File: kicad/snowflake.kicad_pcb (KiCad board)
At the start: 2 copper layers, 123.3 x 86 mm, 62 parts

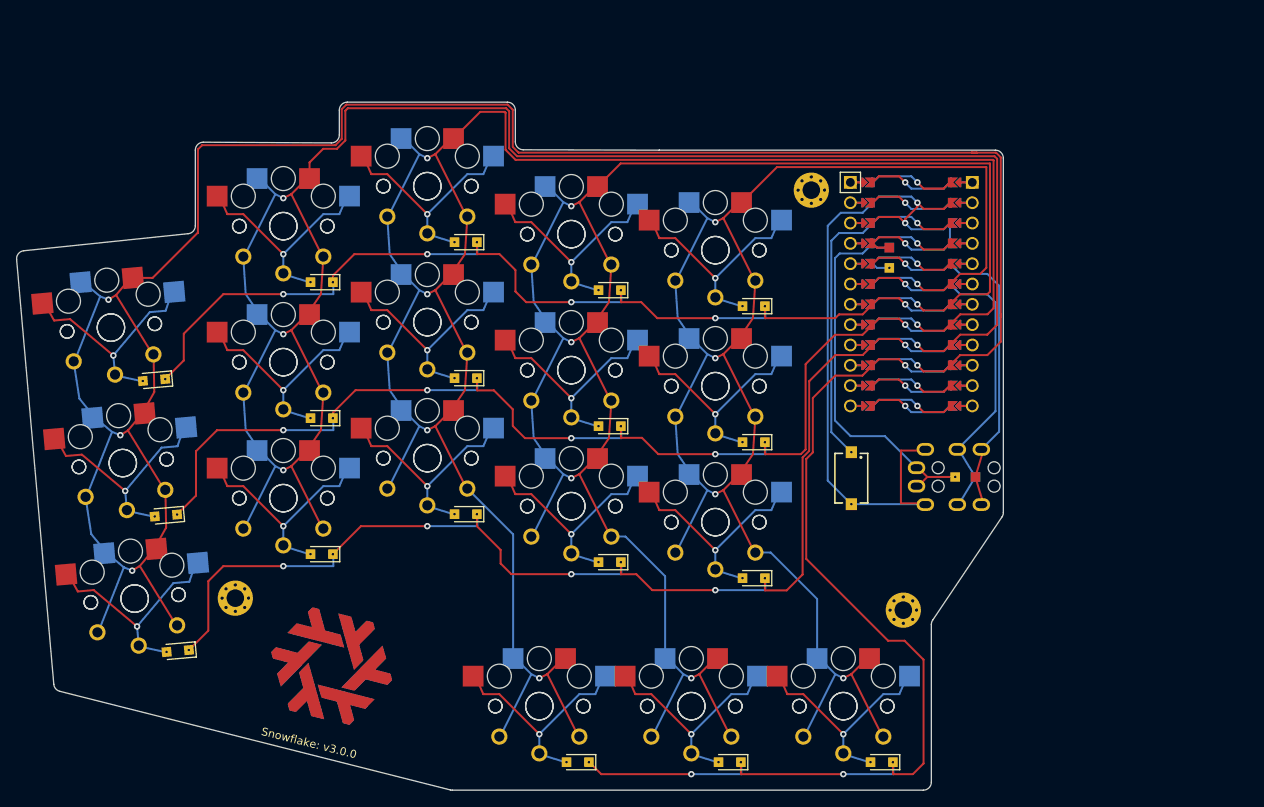
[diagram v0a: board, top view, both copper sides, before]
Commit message: chore: backup
I am not done with these changes but am about to wipe my computer.
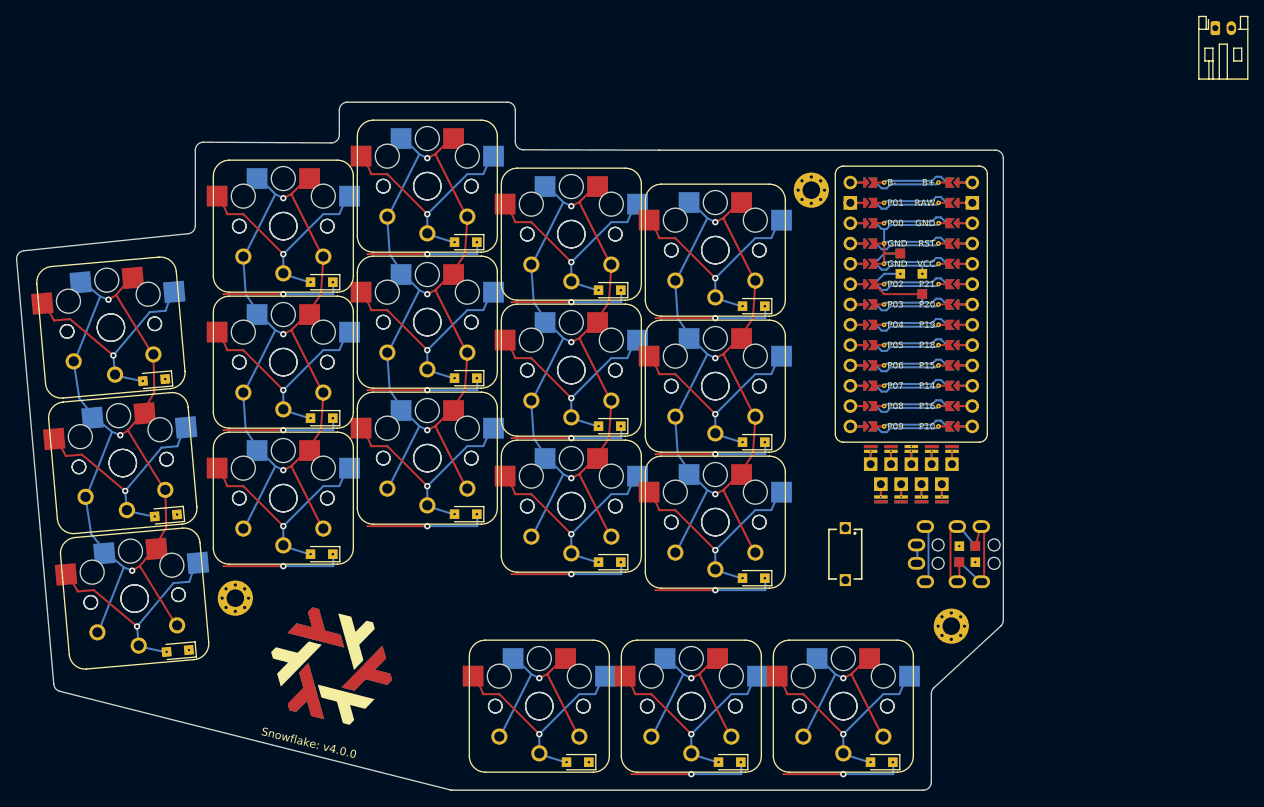
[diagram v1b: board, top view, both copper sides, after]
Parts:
- removed MCU1: , ProMicro
- removed S37: , PG1350
- removed _2, _3: , MountingHole_2.2mm_M2_Pad_Via
- added ?: , 434121025816,  at (188.8, 94.5)
- added ?: , nice!view,  at (197.1, 83.2)
- added ?: , ssd1306,  at (197.1, 85.7)
- added _10: , MountingHole_2.2mm_M2_Pad_Via,  at (202.1, 103.5)
- added _11: , MountingHole_2.2mm_M2_Pad_Via,  at (112.6, 100.0)
- added _9: , MountingHole_2.2mm_M2_Pad_Via,  at (184.6, 49.0)
- added nice!nano1: , nice!nano,  at (197.1, 60.7)
- added threeWayJumper3: Jumper, Jumper_1TH_2SMD, F.Cu at (204.1, 93.5)
- added threeWayJumper4: Jumper, Jumper_1TH_2SMD, F.Cu at (204.1, 95.5)
- D1, D10, D11, D12, D13, D14, D15, D16, D17, D18, D2, D3, D4, D5, D6, D7, D8, D9: moved to 
- S1: footprint 434121025816 -> PG1350
- _1: footprint MountingHole_2.2mm_M2_Pad_Via -> Connector_JST:JST_PH_S2B-PH-K_1x02_P2.00mm_Horizontal; moved to 
- moved S1 90.8 mm to (100.0, 100.0), turned to 5 degrees
- moved S19 89.6 mm to (100.0, 100.0), turned to 185 degrees
- moved S16 61.1 mm to (150.6, 113.5)
- moved S34 61.1 mm to (150.6, 113.5)
- moved _1 54.4 mm to (235.1, 28.7)
- moved S10 43.9 mm to (154.6, 88.5)
- moved S28 43.9 mm to (154.6, 88.5)
- moved S13 40.2 mm to (172.6, 90.5)
- moved S31 40.2 mm to (172.6, 90.5)
- moved S25 34.1 mm to (136.6, 82.5)
- moved S7 34.1 mm to (136.6, 82.5)
- moved S22 30.3 mm to (118.6, 87.5), turned to 180 degrees
- moved S4 30.3 mm to (118.6, 87.5), turned to 0 degrees
- moved threeWayJumper2 24.7 mm to (198.5, 60.7), turned to 270 degrees
- moved S17 19.0 mm to (169.6, 113.5)
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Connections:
- net P4 renamed P08
- net P5 renamed P09
- D1 pad 1: P6 -> P10
- D10 pad 1: P6 -> P10
- D13 pad 1: P6 -> P10
- D16 pad 1: P7 -> P16
- D17 pad 1: P7 -> P16
- D18 pad 1: P7 -> P16
- D4 pad 1: P6 -> P10
- D7 pad 1: P6 -> P10
- S1 pad 1: RST -> P14
- S1 pad 2: GND -> matrix_pinky_bottom
- S10 pad 1: P18 -> P19
- S10 pad 2: matrix_middle_top -> matrix_index_bottom
- S11 pad 2: matrix_index_bottom -> matrix_index_home
- S12 pad 2: matrix_index_home -> matrix_index_top
- S13 pad 1: P19 -> P20
- S13 pad 2: matrix_index_top -> matrix_inner_bottom
- S14 pad 2: matrix_inner_bottom -> matrix_inner_home
- S15 pad 2: matrix_inner_home -> matrix_inner_top
- S16 pad 1: P20 -> P18
- S16 pad 2: matrix_inner_top -> thumbfan_near_thumb
- S17 pad 1: P18 -> P19
- S17 pad 2: thumbfan_near_thumb -> thumbfan_home_thumb
- S18 pad 1: P19 -> P20
- S18 pad 2: thumbfan_home_thumb -> thumbfan_far_thumb
- S19 pad 1: P20 -> P14
- S19 pad 2: thumbfan_far_thumb -> matrix_pinky_bottom
- S2 pad 2: matrix_pinky_bottom -> matrix_pinky_home
- S20 pad 2: matrix_pinky_bottom -> matrix_pinky_home
- S21 pad 2: matrix_pinky_home -> matrix_pinky_top
- S22 pad 1: P14 -> P15
- S22 pad 2: matrix_pinky_top -> matrix_ring_bottom
- S23 pad 2: matrix_ring_bottom -> matrix_ring_home
- S24 pad 2: matrix_ring_home -> matrix_ring_top
- S25 pad 1: P15 -> P18
- S25 pad 2: matrix_ring_top -> matrix_middle_bottom
- S26 pad 2: matrix_middle_bottom -> matrix_middle_home
- S27 pad 2: matrix_middle_home -> matrix_middle_top
- S28 pad 1: P18 -> P19
- S28 pad 2: matrix_middle_top -> matrix_index_bottom
- S29 pad 2: matrix_index_bottom -> matrix_index_home
- S3 pad 2: matrix_pinky_home -> matrix_pinky_top
- S30 pad 2: matrix_index_home -> matrix_index_top
- S31 pad 1: P19 -> P20
- S31 pad 2: matrix_index_top -> matrix_inner_bottom
- S32 pad 2: matrix_inner_bottom -> matrix_inner_home
- S33 pad 2: matrix_inner_home -> matrix_inner_top
- S34 pad 1: P20 -> P18
- S34 pad 2: matrix_inner_top -> thumbfan_near_thumb
- S35 pad 1: P18 -> P19
- S35 pad 2: thumbfan_near_thumb -> thumbfan_home_thumb
- S36 pad 1: P19 -> P20
- S36 pad 2: thumbfan_home_thumb -> thumbfan_far_thumb
- S4 pad 1: P14 -> P15
- S4 pad 2: matrix_pinky_top -> matrix_ring_bottom
- S5 pad 2: matrix_ring_bottom -> matrix_ring_home
- S6 pad 2: matrix_ring_home -> matrix_ring_top
- S7 pad 1: P15 -> P18
- S7 pad 2: matrix_ring_top -> matrix_middle_bottom
- S8 pad 2: matrix_middle_bottom -> matrix_middle_home
- S9 pad 2: matrix_middle_home -> matrix_middle_top
- TRRS1 pad 3: P3 -> D0
- TRRS1 pad 4: P2 -> D1
- _1 pad 1: (no net) -> B+
- threeWayJumper2 pad 2: P2 -> P02
- threeWayJumper2 pad 3: P3 -> P03
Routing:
- net (no net): track 0.00 -> 1446.5 mm
- net P14: track 281.1 -> 0.00 mm, vias 4 -> 3
- net P18: track 266.7 -> 0.00 mm, vias 5 -> 4
- net P15: track 244.4 -> 0.00 mm, vias 4 -> 3
- net P19: track 235.2 -> 0.00 mm, vias 5 -> 4
- net P20: track 212.2 -> 0.00 mm, vias 5 -> 4
- net P6: track 147.2 -> 0.00 mm, vias 5 -> 0
- net P7: track 122.5 -> 0.00 mm, vias 3 -> 0
- net P05: track 0.00 -> 110.0 mm
- net B-: track 0.00 -> 109.9 mm
- net GND: track 104.7 -> 0.00 mm, vias 3 -> 0
- net P09: track 135.5 -> 55.1 mm, vias 5 -> 4
- net P08: track 123.9 -> 55.1 mm, vias 5 -> 4
- net VCC: track 58.0 -> 0.00 mm, vias 1 -> 0
- net P2: track 46.5 -> 0.00 mm, vias 1 -> 0
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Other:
- outline, holes or cut-outs redrawn
- net class Default added: clearance 0.2, trace_width 0.25, via_dia 0.8, via_drill 0.4
- board text added: "Snowflake: v4.0.0"
- board text removed: "Snowflake: v3.0.0"
